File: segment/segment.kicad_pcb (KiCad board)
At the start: 2 copper layers, 84.5 x 67.9 mm, 23 parts, among them J1 Voltage Taps In [1-13], J2 Thermistors In [1-12], J3 Thermistors In [13-24], J4 Voltage Taps Out [1-13], J5 Thermistors Out [1-12], J6 Thermistors Out [13-24]

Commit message: feat(segment): add labels to silkscreen
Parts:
- added G***: LOGO, SUFST:SUFST, B.Cu at (87.0, 79.4)
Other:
- board text added: "1"
- board text added: "12"
- board text added: "13"
- board text added: "19"
- board text added: "20"
- board text added: "24"
- board text added: "7"
- board text added: "8"
- board text added: "BMS Segment Connector"
- board text added: "In"
- board text added: "Out"
- board text added: "Thermistors"
- board text added: "Voltage Taps"
- board text added: "}"

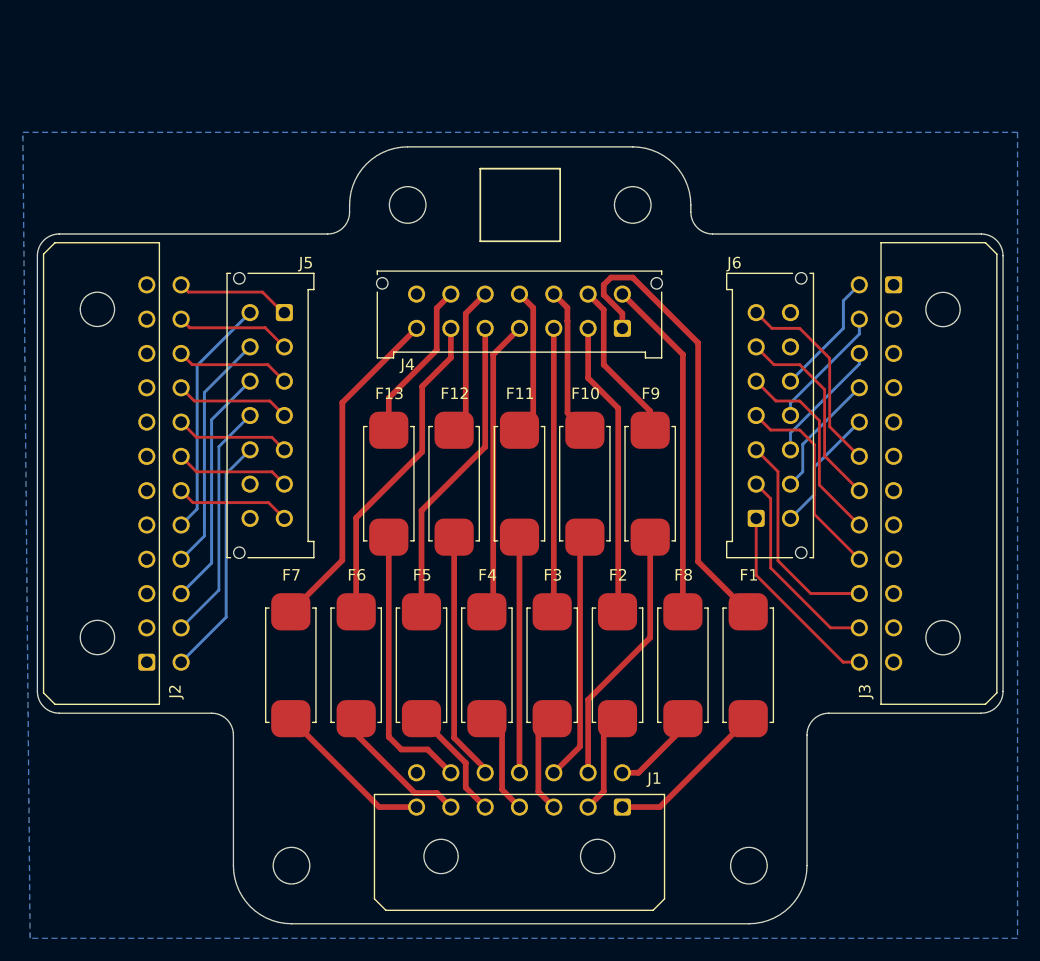
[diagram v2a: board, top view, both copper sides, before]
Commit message: feat(segment): re-do layout to reduce board width
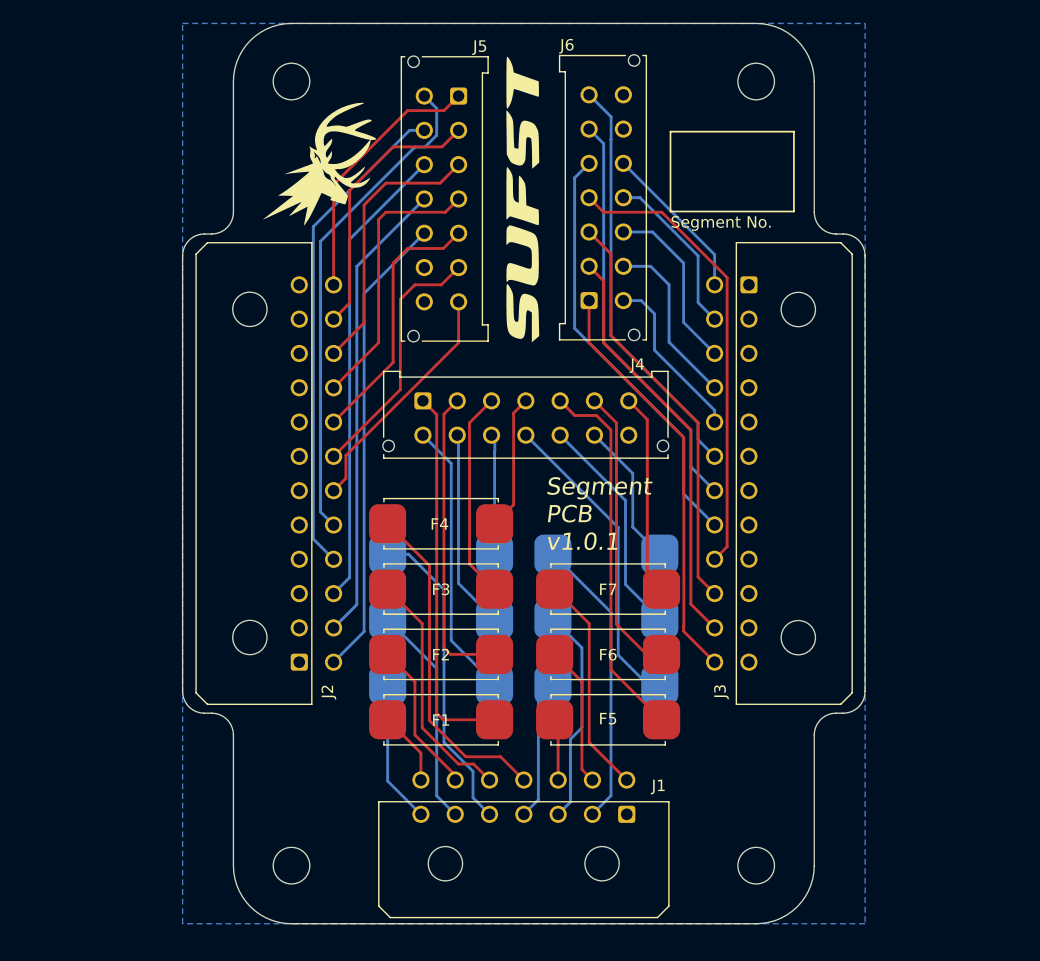
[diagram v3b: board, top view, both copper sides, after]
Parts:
- removed the G*** at (87.0, 79.4)
- added G***: LOGO, LOGO, F.Cu at (69.7, 40.3)
- added G***: LOGO, LOGO, F.Cu at (87.5, 43.3)
- F10, F11, F12, F13, F8, F9: moved to B.Cu
- moved F7 28.7 mm to (95.2, 77.5), turned to 180 degrees
- moved F1 27.1 mm to (80.6, 88.9), turned to 180 degrees
- moved J5 24.3 mm to (81.9, 34.3)
- moved J6 24.0 mm to (93.3, 52.2)
- moved F6 22.2 mm to (95.2, 83.2), turned to 180 degrees
- moved F9 21.7 mm to (80.6, 80.0), turned to 180 degrees
- moved F8 21.0 mm to (80.6, 85.7), turned to 180 degrees
- moved F13 20.2 mm to (95.1, 74.3), turned to 180 degrees
- moved F11 19.4 mm to (95.1, 85.7), turned to 180 degrees
- moved J4 18.6 mm to (78.8, 61.0), turned to 0 degrees
- moved F12 18.1 mm to (95.1, 80.0), turned to 180 degrees
- moved F5 17.3 mm to (95.2, 88.9), turned to 180 degrees
- moved H3 15.3 mm to (108.0, 33.0)
- moved F2 15.3 mm to (80.6, 83.2), turned to 180 degrees
- moved H4 14.8 mm to (67.3, 33.0)
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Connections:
- J1 pad 1: /VTAP_IN_1 -> GND
- J1 pad 10: /VTAP_IN_10 -> /VTAP_IN_5
- J1 pad 11: /VTAP_IN_11 -> /VTAP_IN_4
- J1 pad 12: /VTAP_IN_12 -> /VTAP_IN_3
- J1 pad 13: /VTAP_IN_13 -> /VTAP_IN_2
- J1 pad 14: GND -> /VTAP_IN_1
- J1 pad 2: /VTAP_IN_2 -> /VTAP_IN_13
- J1 pad 3: /VTAP_IN_3 -> /VTAP_IN_12
- J1 pad 4: /VTAP_IN_4 -> /VTAP_IN_11
- J1 pad 5: /VTAP_IN_5 -> /VTAP_IN_10
- J1 pad 6: /VTAP_IN_6 -> /VTAP_IN_9
- J1 pad 7: /VTAP_IN_7 -> /VTAP_IN_8
- J1 pad 8: /VTAP_IN_8 -> /VTAP_IN_7
- J1 pad 9: /VTAP_IN_9 -> /VTAP_IN_6
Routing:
- net /THERM_16: track 17.8 -> 40.1 mm
- net /THERM_8: track 21.1 -> 43.2 mm
- net /THERM_9: track 21.1 -> 43.0 mm
- net /VTAP_IN_4: track 8.91 -> 29.1 mm
- net /THERM_12: track 21.1 -> 40.8 mm
- net /THERM_11: track 21.1 -> 40.8 mm
- net /THERM_10: track 21.1 -> 40.8 mm
- net /THERM_17: track 17.5 -> 37.2 mm
- net /THERM_13: track 17.1 -> 36.2 mm
- net /THERM_18: track 17.6 -> 36.2 mm
- net /THERM_19: track 17.7 -> 36.2 mm
- net /THERM_14: track 17.8 -> 36.2 mm
- net /THERM_15: track 18.8 -> 36.2 mm
- net /VTAP_OUT_11: track 12.9 -> 27.3 mm
- net /VTAP_OUT_4: track 26.0 -> 11.9 mm
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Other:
- board size 84.5 x 67.9 mm -> 59.7 x 78.7 mm
- board text added: "Segment No."
- board text added: "Segment PCB v1.0.1"
- board text removed: "BMS Segment Connector"

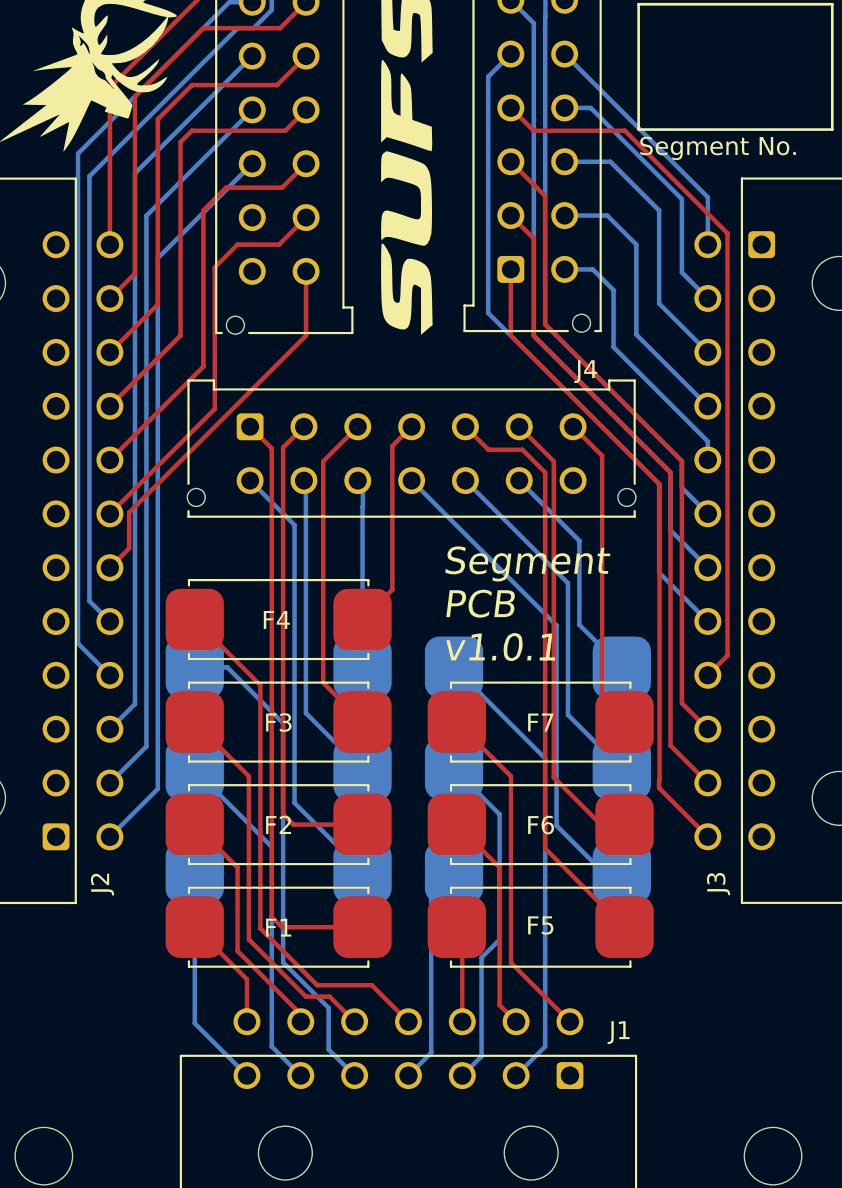
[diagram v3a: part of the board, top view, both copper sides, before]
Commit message: fix(segment): increase trace widths of voltage taps (#27)
* fix(segment): increase trace width for voltage taps

* refactor(segment): improve various bits of routing
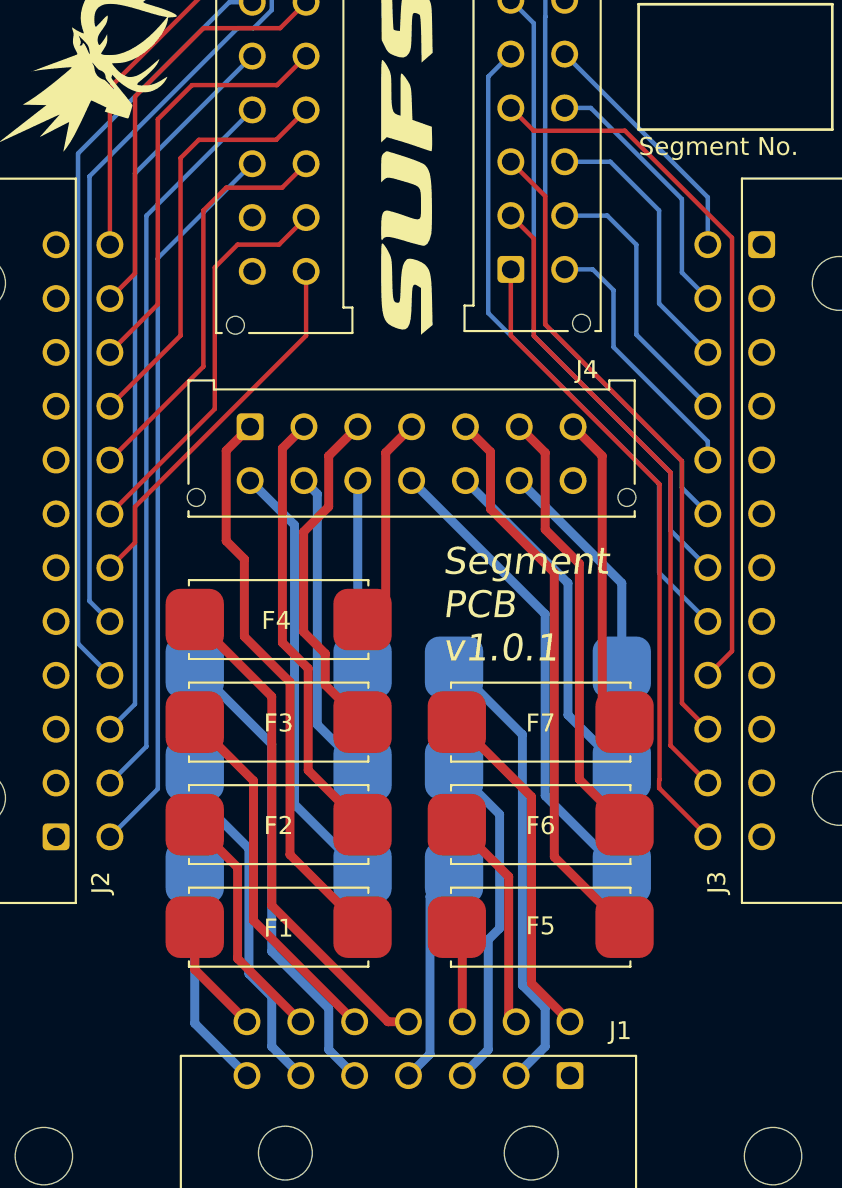
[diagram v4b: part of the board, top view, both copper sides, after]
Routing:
- net /VTAP_OUT_2: track 26.7 -> 24.5 mm
- net /VTAP_OUT_1: track 33.1 -> 31.6 mm
- net /VTAP_OUT_5: track 32.7 -> 31.6 mm
- net /VTAP_IN_4: track 29.1 -> 28.0 mm
- net /VTAP_IN_10: track 27.5 -> 26.4 mm
- net /VTAP_OUT_3: track 18.2 -> 19.1 mm
- net /VTAP_IN_3: track 21.2 -> 20.4 mm
- net /VTAP_OUT_6: track 25.4 -> 24.6 mm
- net /VTAP_OUT_11: track 27.3 -> 26.7 mm
- net /THERM_4: track 24.1 -> 23.6 mm
